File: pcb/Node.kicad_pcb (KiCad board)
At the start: 4 copper layers, 50 x 50 mm, 92 parts, among them J1 LCD, J10 SPI, J13 Power, J14 SERIAL, J2 USB_C_USB2.0_16P, J3 INDICATOR, J4 GPB[0..3], J5 GPB[4..7], J6 BTN_IN, J7 GPA[4..7], J8 QWIIC1, J9 QWIIC2, SW1 RESET, SW2 BOOT, U1 ESP32-S3-WROOM-1-N8R2, U2 LM66200DRLR, U3 USBLC6-2P6, U4 MCP23017_ML, U5 LD1117S33TR_SOT223

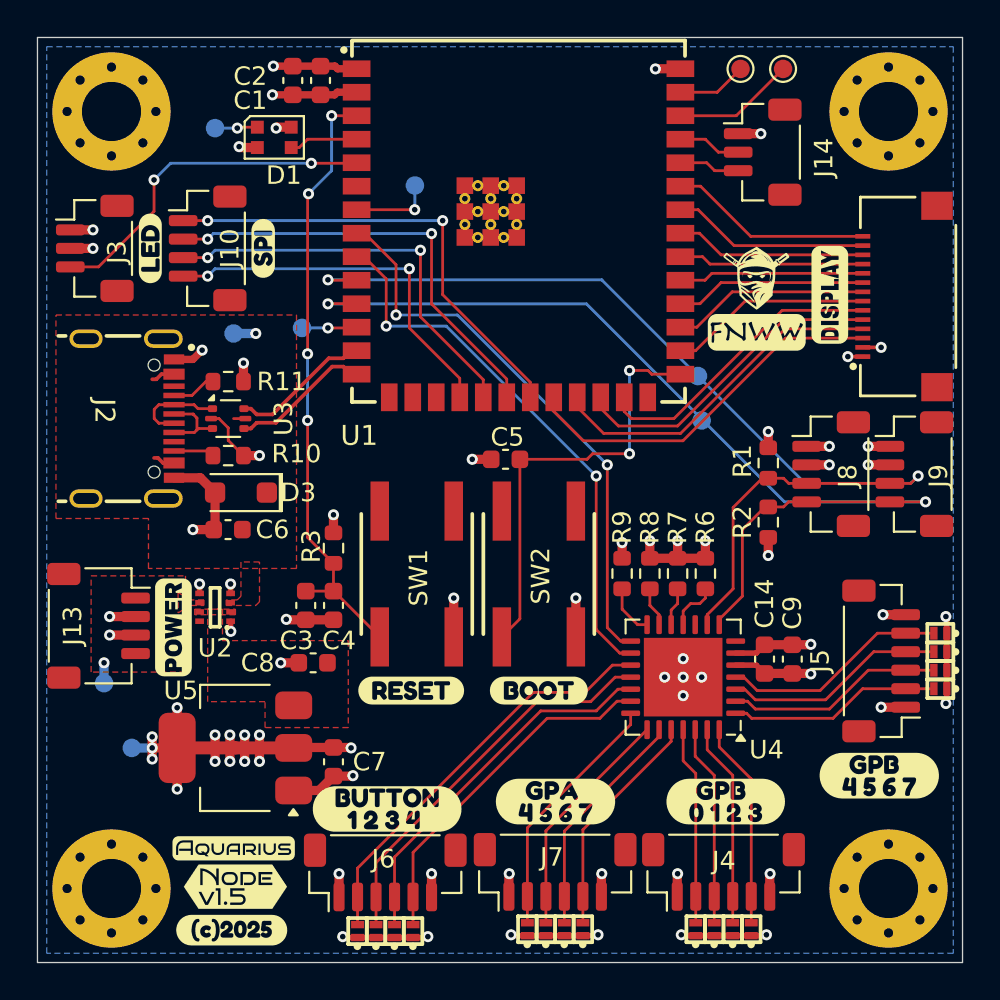
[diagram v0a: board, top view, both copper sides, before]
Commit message: Added buzzer
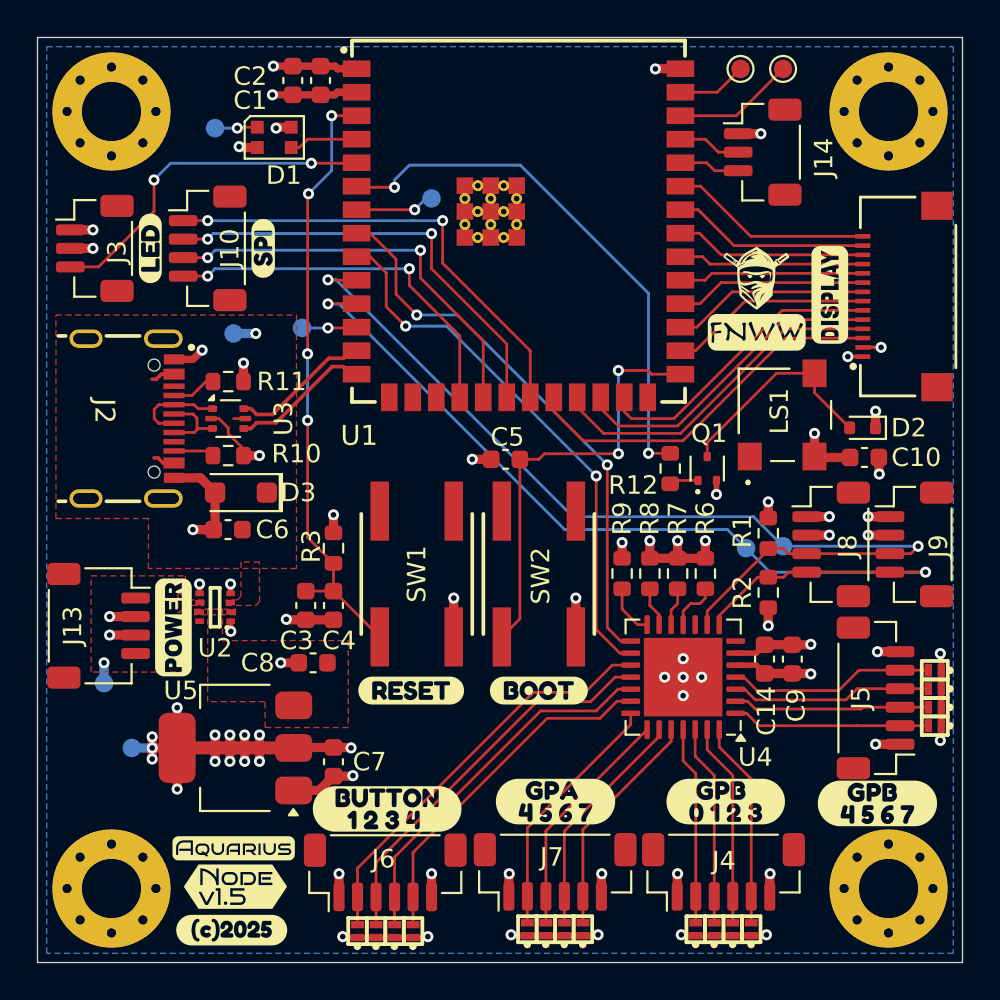
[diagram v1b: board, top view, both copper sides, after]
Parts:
- added C10: 1uF, Capacitor_SMD:C_0603_1608Metric, F.Cu at (104.7, 72.7)
- added D2: D_Schottky, Diode_SMD:D_SOD-523, F.Cu at (104.6, 71.1)
- added LS1: CMT-0502-75-SMT-TR, CRG Makes:CMT050275SMTTR, F.Cu at (100.4, 70.4)
- added Q1: MMBT2222A, Package_TO_SOT_SMD:SOT-523, F.Cu at (96.2, 73.3)
- added R12: 1K, Resistor_SMD:R_0603_1608Metric, F.Cu at (94.2, 73.3)
- moved TP1 10.3 mm to (100.3, 77.5)
- moved kibuzzard-67B9F9C2 10.2 mm to (100.1, 75.9)
- moved kibuzzard-67B9F9CD 7.31 mm to (98.3, 79.2)
- moved TP2 7.31 mm to (98.3, 77.6)
- moved J8 3.80 mm to (102.9, 77.4)
- moved J9 3.80 mm to (107.4, 77.4)
- moved R1 3.80 mm to (99.5, 76.8)
- moved R2 3.80 mm to (99.5, 80.0)
- moved D10 2.02 mm to (108.5, 85.2)
- moved D11 2.02 mm to (108.5, 84.2)
- moved D8 2.02 mm to (108.5, 87.2)
- moved D9 2.02 mm to (108.5, 86.2)
- moved J5 2.02 mm to (105.3, 85.7)
- moved kibuzzard-680D000B 1.50 mm to (105.4, 91.4)
- moved TP7 1.14 mm to (81.3, 58.7)
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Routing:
- net BUZZER: track 0.00 -> 29.2 mm, vias 0 -> 2
- net /Peripherals/BUZZ_GND: track 0.00 -> 11.8 mm
- net +3.3V: track 46.1 -> 50.1 mm, vias 29 -> 31
- net I2C_SDA: track 56.0 -> 53.3 mm
- net I2C_SCL: track 54.5 -> 52.5 mm
- net GND: track 79.6 -> 81.3 mm, vias 44 -> 46
- net Net-(Q1-B): track 0.00 -> 1.57 mm
- net /PIO/GPB7: track 12.3 -> 11.2 mm
- net /PIO/GPB5: track 11.8 -> 10.6 mm
- net /PIO/GPB6: track 12.0 -> 10.9 mm
- net /PIO/GPB4: track 11.5 -> 10.7 mm
- net PIO_INTA: track 30.8 -> 30.2 mm

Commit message: Changed SPI to 8 pin connector
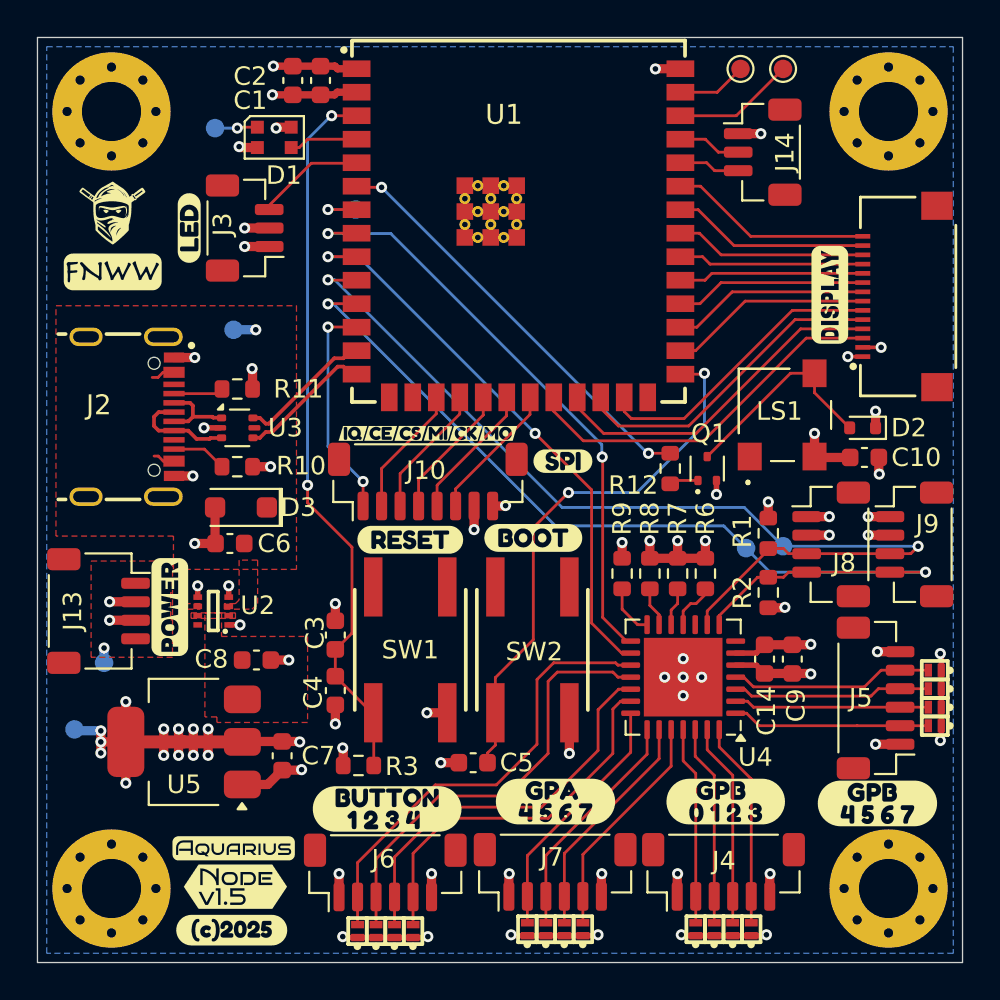
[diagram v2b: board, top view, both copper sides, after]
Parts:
- removed TP9: IO8, TestPoint:TestPoint_Pad_D1.0mm
- removed kibuzzard-68103482: G***, kibuzzard-68103482
- added kibuzzard-6812E37E: G***, kibuzzard-6812E37E, F.Cu at (78.5, 71.4)
- added kibuzzard-6812E3A0: G***, kibuzzard-6812E3A0, F.Cu at (80.2, 71.4)
- added kibuzzard-6812E3AD: G***, kibuzzard-6812E3AD, F.Cu at (81.7, 71.4)
- added kibuzzard-6812E3BB: G***, kibuzzard-6812E3BB, F.Cu at (83.2, 71.4)
- added kibuzzard-6812E3C5: G***, kibuzzard-6812E3C5, F.Cu at (84.9, 71.4)
- added kibuzzard-6812E420: G***, kibuzzard-6812E420, F.Cu at (77.0, 71.4)
- J10: footprint CRGM Connector:JST_SH_BM04B-SRSS-TB_1x04-1MP_P1.00mm_Vertical -> Connector_JST:JST_SH_BM08B-SRSS-TB_1x08-1MP_P1.00mm_Vertical
- moved kibuzzard-680D01D7 19.9 mm to (88.4, 72.9), turned to 0 degrees
- moved J10 17.3 mm to (81.1, 74.0), turned to 0 degrees
- moved C5 16.5 mm to (83.5, 89.2)
- moved R3 11.8 mm to (77.3, 89.3), turned to 0 degrees
- moved kibuzzard-680D06A5 8.26 mm to (86.8, 77.0)
- moved J3 8.17 mm to (71.2, 60.3), turned to 90 degrees
- moved kibuzzard-680D069E 8.15 mm to (80.2, 77.2)
- moved LOGO2 7.02 mm to (80.1, 73.4)
- moved LOGO1 6.46 mm to (89.6, 72.7)
- moved C4 4.60 mm to (76.1, 85.3)
- moved kibuzzard-6810346D 4.46 mm to (76.8, 57.9)
- moved kibuzzard-681034B6 4.18 mm to (67.0, 83.8)
- moved TP7 4.14 mm to (77.2, 59.3)
- moved SW1 4.11 mm to (80.2, 83.1)
- moved SW2 4.11 mm to (86.8, 83.1)
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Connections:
- J10 pad 1: SPI_MOSI -> SPI_IRQ0
- J10 pad 2: SPI_CLK -> SPI_CE0
- J10 pad 3: SPI_MISO -> SPI_CS0
- J10 pad 4: SPI_CS0 -> SPI_MISO
- U1 pad 12: Net-(U1-IO8) -> SPI_IRQ0
- U1 pad 17: SPI_CS1 -> SPI_CE0
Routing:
- net SPI_MOSI: track 25.5 -> 7.55 mm, vias 2 -> 0
- net SPI_CLK: track 24.1 -> 7.43 mm, vias 2 -> 0
- net SPI_MISO: track 22.3 -> 7.32 mm, vias 2 -> 0
- net SPI_CS0: track 20.5 -> 7.21 mm, vias 2 -> 0
- net LEDS: track 18.8 -> 5.90 mm, vias 2 -> 0
- net SPI_IRQ0: track 0.00 -> 12.1 mm, vias 0 -> 2
- net SPI_CE0: track 0.00 -> 7.10 mm
- net BUZZER: track 29.2 -> 22.9 mm
- net BOOT: track 23.5 -> 29.5 mm
- net EN: track 33.5 -> 39.3 mm, vias 4 -> 2
- net GND: track 81.3 -> 77.5 mm, vias 46 -> 50
- net Net-(U1-IO8): track 2.97 -> 0.00 mm, vias 1 -> 0
- net /PIO/BTN2: track 21.3 -> 23.9 mm
- net /PIO/BTN1: track 22.4 -> 24.7 mm
- net PIO_INTA: track 30.2 -> 32.5 mm
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
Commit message: Added additional labels; minor clean up.
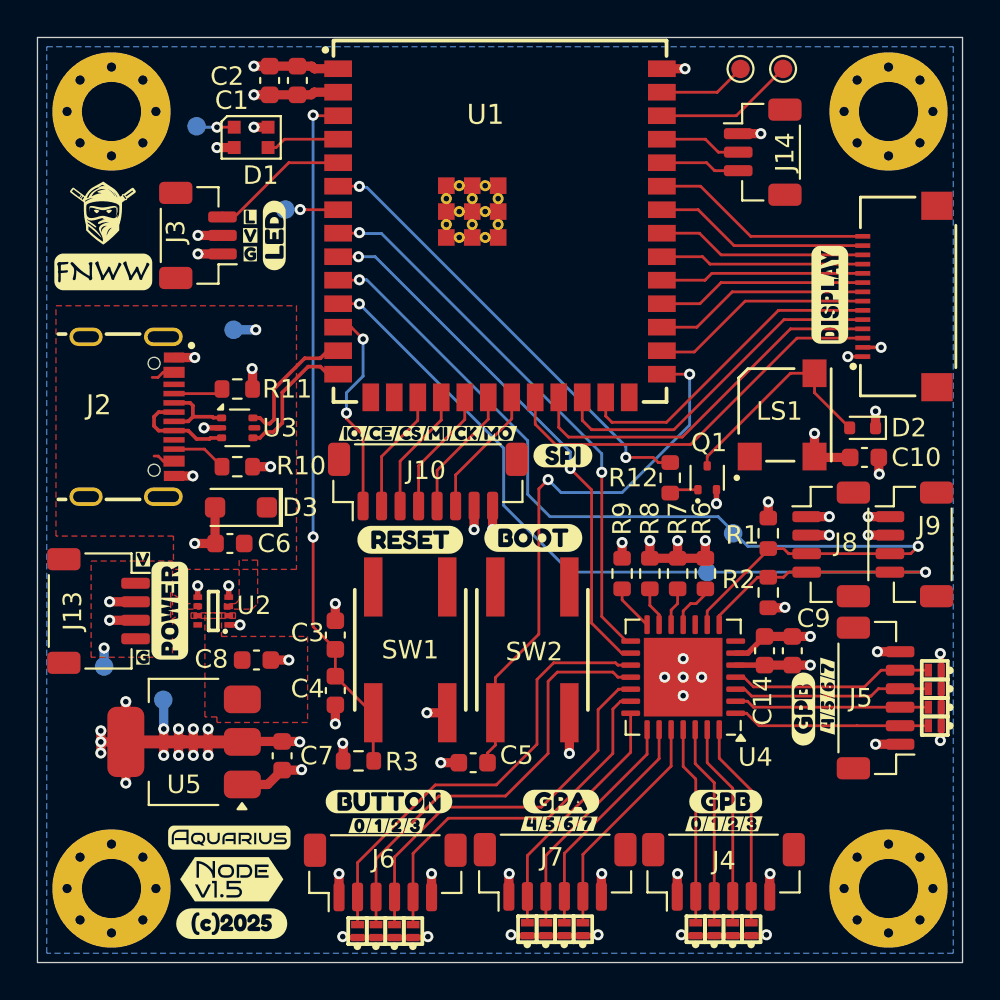
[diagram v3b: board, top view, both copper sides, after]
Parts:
- removed kibuzzard-680D000B: G***, kibuzzard-680D000B
- removed kibuzzard-680D0021: G***, kibuzzard-680D0021
- removed kibuzzard-680D0065: G***, kibuzzard-680D0065
- removed kibuzzard-680D0321: G***, kibuzzard-680D0321
- added kibuzzard-68142030: G***, kibuzzard-68142030, F.Cu at (89.7, 92.5)
- added kibuzzard-68142030: G***, kibuzzard-68142030, F.Cu at (102.7, 84.1)
- added kibuzzard-68142039: G***, kibuzzard-68142039, F.Cu at (88.7, 92.5)
- added kibuzzard-68142039: G***, kibuzzard-68142039, F.Cu at (102.7, 85.1)
- added kibuzzard-68142043: G***, kibuzzard-68142043, F.Cu at (87.7, 92.5)
- added kibuzzard-68142043: G***, kibuzzard-68142043, F.Cu at (102.7, 86.1)
- added kibuzzard-6814204F: G***, kibuzzard-6814204F, F.Cu at (102.7, 87.1)
- added kibuzzard-6814204F: G***, kibuzzard-6814204F, F.Cu at (86.7, 92.5)
- added kibuzzard-681420CD: G***, kibuzzard-681420CD, F.Cu at (95.6, 92.5)
- added kibuzzard-681420CD: G***, kibuzzard-681420CD, F.Cu at (77.4, 92.6)
- added kibuzzard-681420D1: G***, kibuzzard-681420D1, F.Cu at (78.4, 92.6)
- added kibuzzard-681420D1: G***, kibuzzard-681420D1, F.Cu at (96.6, 92.5)
- added kibuzzard-681420D5: G***, kibuzzard-681420D5, F.Cu at (97.6, 92.5)
- added kibuzzard-681420D5: G***, kibuzzard-681420D5, F.Cu at (79.4, 92.6)
- added kibuzzard-681420DA: G***, kibuzzard-681420DA, F.Cu at (80.4, 92.6)
- added kibuzzard-681420DA: G***, kibuzzard-681420DA, F.Cu at (98.6, 92.5)
- added kibuzzard-681420E9: G***, kibuzzard-681420E9, F.Cu at (79.0, 91.3)
- added kibuzzard-681420F3: G***, kibuzzard-681420F3, F.Cu at (88.3, 91.3)
- added kibuzzard-68142110: G***, kibuzzard-68142110, F.Cu at (97.2, 91.3)
- added kibuzzard-6814212B: G***, kibuzzard-6814212B, F.Cu at (101.4, 86.3)
- added kibuzzard-6814216F: G***, kibuzzard-6814216F, F.Cu at (65.7, 78.2)
- added kibuzzard-6814217B: G***, kibuzzard-6814217B, F.Cu at (65.7, 83.5)
- added kibuzzard-68142199: G***, kibuzzard-68142199, F.Cu at (71.5, 59.7)
- added kibuzzard-681421A1: G***, kibuzzard-681421A1, F.Cu at (71.5, 60.7)
- added kibuzzard-681421A9: G***, kibuzzard-681421A9, F.Cu at (71.5, 61.7)
- moved LOGO2 11.1 mm to (89.9, 68.2)
- moved LOGO1 11.1 mm to (99.0, 66.9)
- moved kibuzzard-681035B7 7.50 mm to (69.6, 85.8)
- moved kibuzzard-68103896 5.48 mm to (87.1, 85.9)
- moved TP8 5.06 mm to (66.8, 85.8)
- moved kibuzzard-68103881 4.92 mm to (86.5, 82.1)
- moved kibuzzard-680D0262 4.62 mm to (72.8, 60.7)
- moved TP7 3.80 mm to (73.4, 59.3)
- moved TP1 2.79 mm to (97.6, 76.8)
- moved J3 2.56 mm to (68.7, 60.7)
- moved TP2 2.47 mm to (96.2, 78.9)
- moved C1 1.25 mm to (74.0, 52.3)
- moved C2 1.25 mm to (72.5, 52.3)
- moved D1 1.25 mm to (71.5, 55.4)
- moved TP3 1.00 mm to (68.6, 54.8)
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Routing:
- net PIO_INTA: track 32.5 -> 30.1 mm
- net LCD_RS: track 19.0 -> 20.8 mm
- net LEDS: track 5.90 -> 7.69 mm
- net BUZZER: track 22.9 -> 24.5 mm
- net LCD_CS: track 20.5 -> 22.1 mm
- net PIO_INTB: track 31.0 -> 29.4 mm
- net LCD_DC: track 17.6 -> 19.2 mm
- net EN: track 39.3 -> 38.0 mm
- net LCD_SDI: track 16.3 -> 17.7 mm
- net LCD_SCK: track 11.1 -> 12.2 mm
- net T_SDA: track 10.4 -> 11.4 mm
- net T_SCL: track 10.1 -> 11.1 mm
- net T_RESET: track 10.1 -> 11.1 mm
- net T_INT: track 10.8 -> 11.8 mm
- net TX: track 3.41 -> 4.41 mm
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
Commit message: added open hw; changed test points; added pulls on buttons
change buttons to be 2 connectors with pull ups.
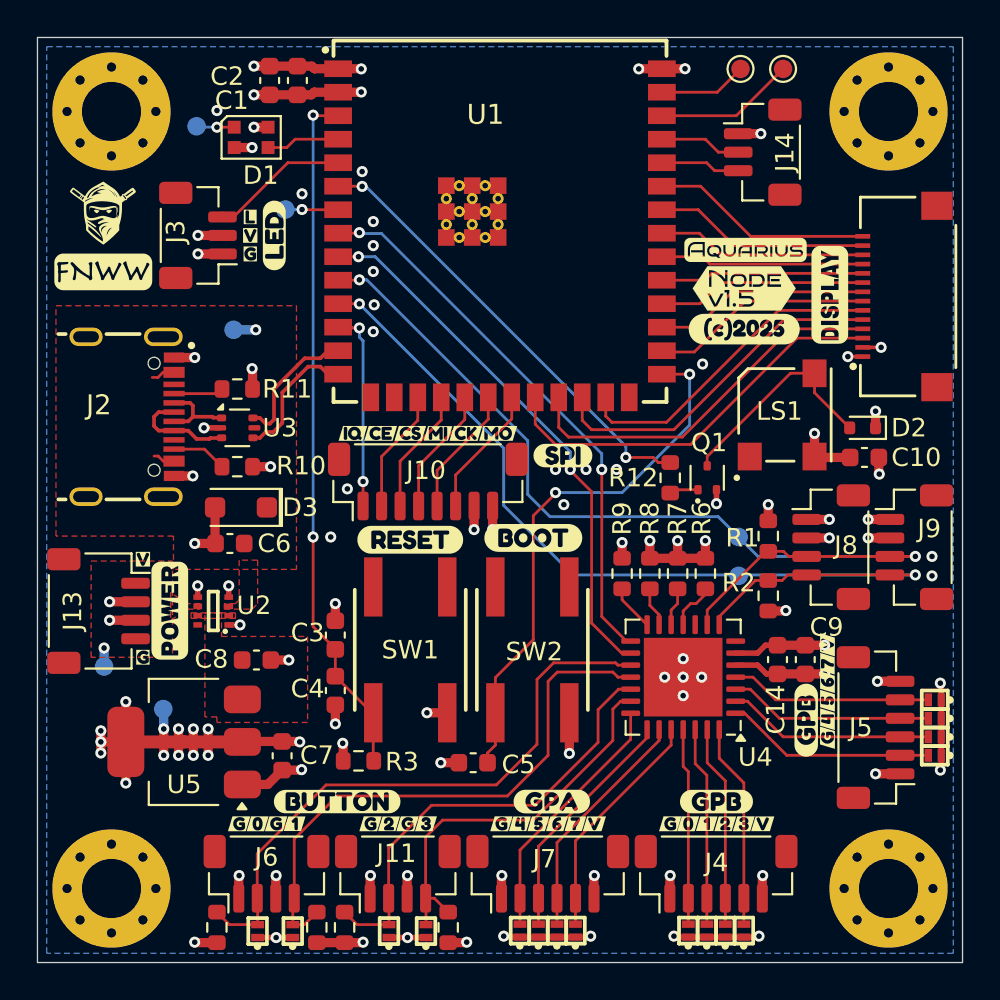
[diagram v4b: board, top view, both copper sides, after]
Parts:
- removed the kibuzzard-681420CD at (77.4, 92.6)
- removed the kibuzzard-681420D1 at (78.4, 92.6)
- removed the kibuzzard-681420D5 at (79.4, 92.6)
- added J11: ~, CRGM Connector:JST_SH_BM04B-SRSS-TB_1x04-1MP_P1.00mm_Vertical, F.Cu at (79.5, 95.2)
- added LOGO3: Logo_Open_Hardware_Small, Symbol:OSHW-Logo_5.7x6mm_SilkScreen, B.Cu at (71.5, 91.8)
- added R13: 10K, Resistor_SMD:R_0603_1608Metric, F.Cu at (75.1, 98.1)
- added R14: 10K, Resistor_SMD:R_0603_1608Metric, F.Cu at (69.7, 98.1)
- added R4: 10K, Resistor_SMD:R_0603_1608Metric, F.Cu at (82.2, 98.1)
- added R5: 10K, Resistor_SMD:R_0603_1608Metric, F.Cu at (76.6, 98.1)
- added kibuzzard-68153CC4: G***, kibuzzard-68153CC4, F.Cu at (85.1, 92.5)
- added kibuzzard-68153CC4: G***, kibuzzard-68153CC4, F.Cu at (78.0, 92.5)
- added kibuzzard-68153CC4: G***, kibuzzard-68153CC4, F.Cu at (94.2, 92.5)
- added kibuzzard-68153CC9: G***, kibuzzard-68153CC9, F.Cu at (79.0, 92.5)
- added kibuzzard-68153CCE: G***, kibuzzard-68153CCE, F.Cu at (80.0, 92.5)
- added kibuzzard-68153CDD: G***, kibuzzard-68153CDD, F.Cu at (70.9, 92.5)
- added kibuzzard-68153CE4: G***, kibuzzard-68153CE4, F.Cu at (71.9, 92.5)
- added kibuzzard-68153CEB: G***, kibuzzard-68153CEB, F.Cu at (72.9, 92.5)
- added kibuzzard-68153CEF: G***, kibuzzard-68153CEF, F.Cu at (73.9, 92.5)
- added kibuzzard-6815408B: G***, kibuzzard-6815408B, F.Cu at (102.7, 87.8)
- added kibuzzard-68154095: G***, kibuzzard-68154095, F.Cu at (102.7, 82.8)
- added kibuzzard-68154095: G***, kibuzzard-68154095, F.Cu at (90.1, 92.5)
- added kibuzzard-68154095: G***, kibuzzard-68154095, F.Cu at (99.2, 92.5)
- J6: value BTN_IN -> ~; footprint CRGM Connector:JST_SH_BM06B-SRSS-TB_1x06-1MP_P1.00mm_Vertical -> CRGM Connector:JST_SH_BM04B-SRSS-TB_1x04-1MP_P1.00mm_Vertical
- TP1, TP10, TP2, TP3, TP4, TP7, TP8: footprint TestPoint:TestPoint_Pad_D1.0mm -> CRGM Mechanical:TestPoint_Pad_D1.0mm
- moved kibuzzard-680D0826 42.4 mm to (98.2, 65.8)
- moved kibuzzard-67B9FE41 42.3 mm to (98.2, 63.6)
- moved LOGO1 8.01 mm to (91.8, 70.4)
- moved LOGO2 7.96 mm to (82.9, 72.0)
- moved J6 6.42 mm to (72.4, 95.2)
- moved D12 5.40 mm to (71.9, 98.3)
- moved D13 4.50 mm to (73.8, 98.3)
- moved kibuzzard-68103456 2.98 mm to (68.9, 56.3)
- moved kibuzzard-681420E9 2.80 mm to (76.2, 91.3)
- moved kibuzzard-68103881 1.81 mm to (86.7, 80.3)
- moved TP2 1.71 mm to (97.9, 79.1)
- moved D10 1.60 mm to (108.5, 86.8)
- moved D11 1.60 mm to (108.5, 85.8)
- moved D8 1.60 mm to (108.5, 88.8)
- moved D9 1.60 mm to (108.5, 87.8)
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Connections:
- D12 pad 2: /PIO/BTN1 -> /PIO/BTN0
- D13 pad 2: /PIO/BTN2 -> /PIO/BTN1
- D14 pad 2: /PIO/BTN3 -> /PIO/BTN2
- D15 pad 2: /PIO/BTN4 -> /PIO/BTN3
- J6 pad 2: /PIO/BTN1 -> /PIO/BTN0
- J6 pad 3: /PIO/BTN2 -> GND
- J6 pad 4: /PIO/BTN3 -> /PIO/BTN1
- U4 pad 17: /PIO/BTN1 -> /PIO/BTN0
- U4 pad 18: /PIO/BTN2 -> /PIO/BTN1
- U4 pad 19: /PIO/BTN3 -> /PIO/BTN2
- U4 pad 20: /PIO/BTN4 -> /PIO/BTN3
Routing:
- net /PIO/BTN0: track 0.00 -> 32.9 mm
- net /PIO/BTN4: track 20.4 -> 0.00 mm
- net GND: track 77.5 -> 83.6 mm, vias 50 -> 72
- net /PIO/BTN1: track 24.7 -> 30.6 mm
- net +3.3V: track 51.7 -> 56.8 mm, vias 32 -> 35
- net BOOT: track 30.4 -> 29.2 mm
- net I2C_SCL: track 52.2 -> 51.1 mm
- net /PIO/GPB5: track 10.5 -> 11.2 mm
- net /PIO/GPB4: track 10.7 -> 11.4 mm
- net /PIO/BTN2: track 23.9 -> 24.5 mm
- net SPI_IRQ0: track 11.4 -> 10.9 mm
